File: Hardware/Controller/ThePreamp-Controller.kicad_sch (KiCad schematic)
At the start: 12 parts, among them J1 8V, J2 Digital Out, J3 SPI DISPLAY 1, J4 SPI DISPLAY 2, J5 Power relay trigger, SW1 RotaryEncoder_Switch, SW2 RotaryEncoder_Switch, U1 24C02C_SN, U2 ESP32-DEVKIT-V1, U3 TSOP34838, U4 PC817

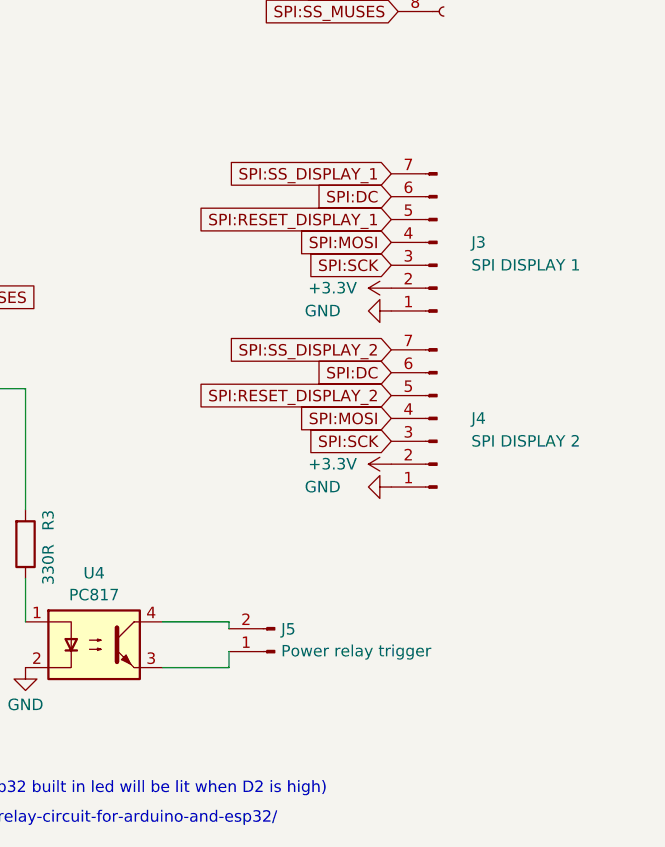
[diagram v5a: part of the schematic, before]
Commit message: Added symbol/footprint for display
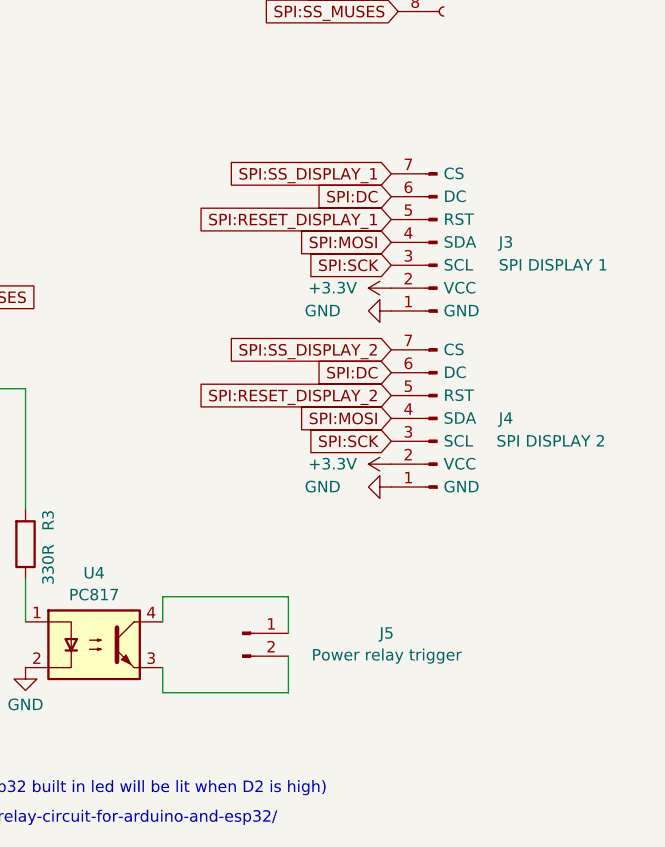
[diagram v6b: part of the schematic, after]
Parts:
- J3, J4: footprint Connector_PinHeader_2.54mm:PinHeader_1x07_P2.54mm_Vertical -> OLED SPI 2.08:OLED SPI 2.08; symbol Connector:Conn_01x07_Pin -> OLED SPI 2.08:OLED SPI 2.08
- J5: footprint Connector_JST:JST_XH_B2B-XH-AM_1x02_P2.50mm_Vertical -> Connector_JST:JST_XH_B2B-XH-A_1x02_P2.50mm_Vertical
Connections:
- net at U4.3: now also J5.2 (Pin_2); no longer J5.1 (Pin_1)
- net at U4.4: now also J5.1 (Pin_1); no longer J5.2 (Pin_2)
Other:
- moved on the sheet: J5
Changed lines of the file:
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@@
   (no_connect (at 157.48 76.2))
   (no_connect (at 157.48 73.66))
+  (wire (pts (xy 230.886 128.778) (xy 230.886 124.714))
+    (stroke (width 0) (type default))
+  )
   (wire (pts (xy 187.96 101.6) (xy 201.676 101.6))
     (stroke (width 0) (type default))
   )
-  (wire (pts (xy 216.916 127.508) (xy 224.282 127.508))
+  (wire (pts (xy 230.886 135.382) (xy 230.886 131.318))
     (stroke (width 0) (type default))
   )
@@
     (stroke (width 0) (type default))
   )
+  (wire (pts (xy 216.916 135.382) (xy 230.886 135.382))
+    (stroke (width 0) (type default))
+  )
   (wire (pts (xy 100.33 35.56) (xy 100.33 34.29))
     (stroke (width 0) (type default))
   )
+  (wire (pts (xy 216.916 124.714) (xy 230.886 124.714))
+    (stroke (width 0) (type default))
+  )
+  (wire (pts (xy 216.916 124.714) (xy 216.916 127.508))
+    (stroke (width 0) (type default))
+  )
   (wire (pts (xy 158.496 55.372) (xy 158.496 52.832))
     (stroke (width 0) (type default))
   )
-  (wire (pts (xy 224.282 130.81) (xy 224.282 132.588))
-    (stroke (width 0) (type default))
-  )
   (wire (pts (xy 158.496 50.292) (xy 158.496 52.832))
     (stroke (width 0) (type default))
@@
     (stroke (width 0) (type default))
   )
-  (wire (pts (xy 224.282 132.588) (xy 216.916 132.588))
-    (stroke (width 0) (type default))
-  )
   (wire (pts (xy 102.87 34.29) (xy 102.87 35.56))
     (stroke (width 0) (type default))
@@
     (stroke (width 0) (type default))
   )
-  (wire (pts (xy 224.282 127.508) (xy 224.282 128.27))
+  (wire (pts (xy 216.916 132.588) (xy 216.916 135.382))
     (stroke (width 0) (type default))
   )
@@
     )
   )
-  (symbol (lib_id "Connector:Conn_01x07_Pin") (at 247.396 85.344 180) (unit 1)
-    (in_bom yes) (on_board yes) (dnp no)
-    (property "Reference" "J3" (at 251.206 85.344 0)
-      (effects (font (size 1.27 1.27)) (justify right))
-    )
-    (property "Value" "SPI DISPLAY 1" (at 251.206 87.884 0)
-      (effects (font (size 1.27 1.27)) (justify right))
-    )
-    (property "Footprint" "Connector_PinHeader_2.54mm:PinHeader_1x07_P2.54mm_Vertical" (at 247.396 85.344 0)
+  (symbol (lib_id "OLED SPI 2.08:OLED SPI 2.08") (at 247.396 85.344 180) (unit 1)
+    (in_bom yes) (on_board yes) (dnp no)
+    (property "Reference" "J3" (at 254.254 85.344 0)
+      (effects (font (size 1.27 1.27)) (justify right))
+    )
+    (property "Value" "SPI DISPLAY 1" (at 254.254 87.884 0)
+      (effects (font (size 1.27 1.27)) (justify right))
+    )
+    (property "Footprint" "OLED SPI 2.08:OLED SPI 2.08" (at 223.266 75.184 0)
       (effects (font (size 1.27 1.27)) hide)
     )
@@
     )
   )
-  (symbol (lib_id "Connector:Conn_01x02_Pin") (at 229.362 130.81 180) (unit 1)
-    (in_bom yes) (on_board yes) (dnp no) (fields_autoplaced)
-    (property "Reference" "J5" (at 230.0732 128.3279 0)
-      (effects (font (size 1.27 1.27)) (justify right))
-    )
-    (property "Value" "Power relay trigger" (at 230.0732 130.7521 0)
-      (effects (font (size 1.27 1.27)) (justify right))
-    )
-    (property "Footprint" "Connector_JST:JST_XH_B2B-XH-AM_1x02_P2.50mm_Vertical" (at 229.362 130.81 0)
-      (effects (font (size 1.27 1.27)) hide)
-    )
-    (property "Datasheet" "~" (at 229.362 130.81 0)
+  (symbol (lib_id "Connector:Conn_01x02_Pin") (at 225.806 128.778 0) (unit 1)
+    (in_bom yes) (on_board yes) (dnp no)
+    (property "Reference" "J5" (at 241.808 128.778 0)
+      (effects (font (size 1.27 1.27)))
+    )
+    (property "Value" "Power relay trigger" (at 241.808 131.2022 0)
+      (effects (font (size 1.27 1.27)))
+    )
+    (property "Footprint" "Connector_JST:JST_XH_B2B-XH-A_1x02_P2.50mm_Vertical" (at 225.806 128.778 0)
+      (effects (font (size 1.27 1.27)) hide)
+    )
+    (property "Datasheet" "~" (at 225.806 128.778 0)
       (effects (font (size 1.27 1.27)) hide)
     )
@@
     )
   )
-  (symbol (lib_id "Connector:Conn_01x07_Pin") (at 247.396 104.902 180) (unit 1)
-    (in_bom yes) (on_board yes) (dnp no)
-    (property "Reference" "J4" (at 251.206 104.902 0)
-      (effects (font (size 1.27 1.27)) (justify right))
-    )
-    (property "Value" "SPI DISPLAY 2" (at 251.206 107.442 0)
-      (effects (font (size 1.27 1.27)) (justify right))
-    )
-    (property "Footprint" "Connector_PinHeader_2.54mm:PinHeader_1x07_P2.54mm_Vertical" (at 247.396 104.902 0)
-      (effects (font (size 1.27 1.27)) hide)
-    )
+  (symbol (lib_id "OLED SPI 2.08:OLED SPI 2.08") (at 247.396 104.902 180) (unit 1)
+    (in_bom yes) (on_board yes) (dnp no)
+    (property "Reference" "J4" (at 254.254 104.902 0)
+      (effects (font (size 1.27 1.27)) (justify right))
+    )
+    (property "Value" "SPI DISPLAY 2" (at 254 107.442 0)
+      (effects (font (size 1.27 1.27)) (justify right))
+    )
+    (property "Footprint" "OLED SPI 2.08:OLED SPI 2.08" (at 223.266 94.742 0)
+      (effects (font (size 1.27 1.27)) hide)
+    )

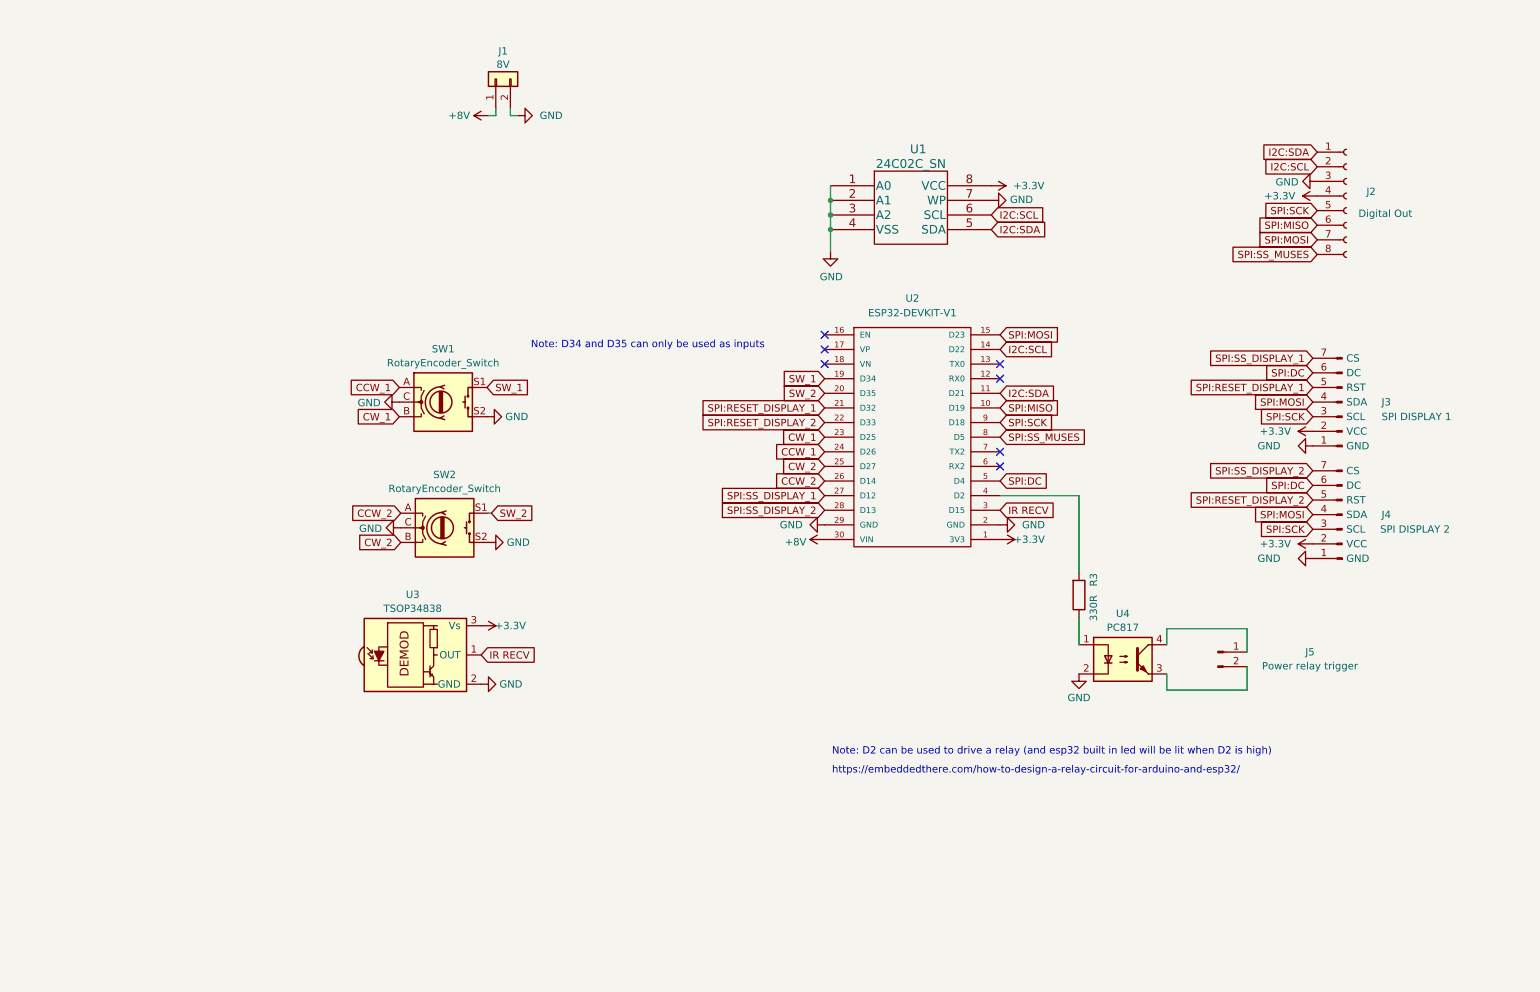
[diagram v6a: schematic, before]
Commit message: Controller pcb is ready (except for connectors)
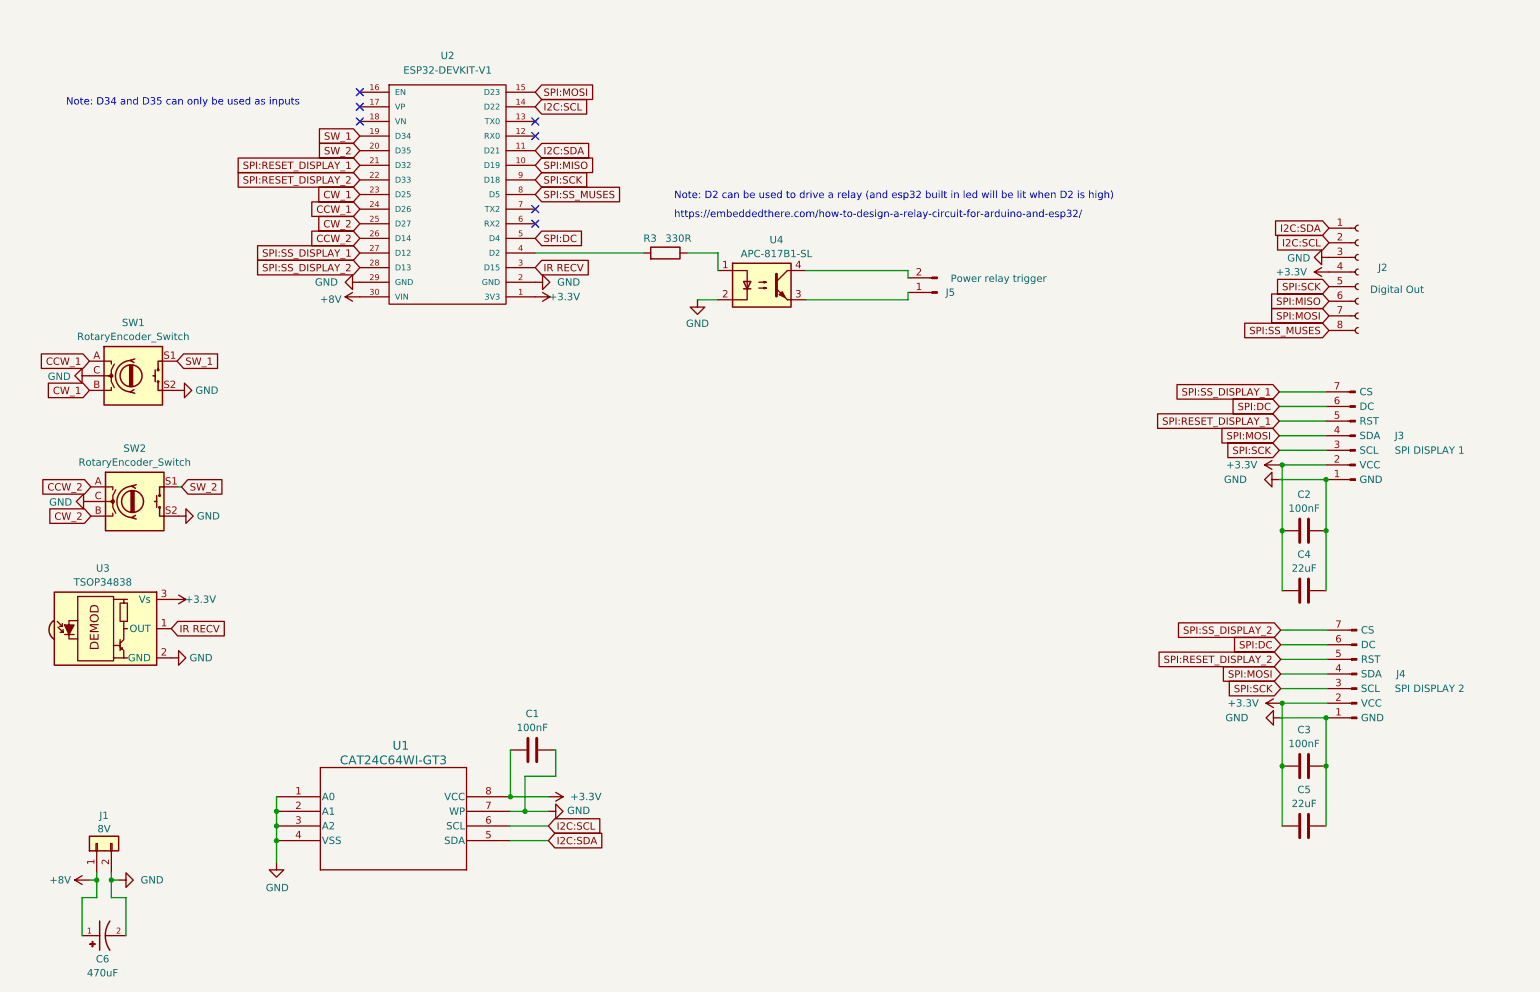
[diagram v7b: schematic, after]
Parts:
- added C1, C2, C3: 100nF, Capacitor_SMD:C_0805_2012Metric_Pad1.18x1.45mm_HandSolder, symbol Device:C
- added C4, C5: 22uF, Capacitor_SMD:C_1206_3216Metric_Pad1.33x1.80mm_HandSolder, symbol Device:C
- added C6: 470uF, EEE_FH1C471L:CAP_EEEFH1C471L, symbol EEE_FH1C471L:EEEFH1C471L
- U1: value 24C02C_SN -> CAT24C64WI-GT3; footprint Package_SO:SOIC-8-1EP_3.9x4.9mm_P1.27mm_EP2.41x3.3mm -> footprints:SOIC8_ONS-M; symbol Mezmerize_B1_Controller-rescue:24C02C_SN-24C02 -> CAT24C64WI_GT3:CAT24C64WI-GT3
- U4: value PC817 -> APC-817B1-SL; footprint Package_DIP:DIP-4_W7.62mm -> APC_817B1_SL:APC-817xx-SL_AMB-M
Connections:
- net +3V3: now also C1.1, C2.1, C3.1, C4.1, C5.1
- net +8V: now also C6.1
- net GND: now also C1.2, C2.2, C3.2, C4.2, C5.2, C6.2
- net at U4.3: now also J5.1 (Pin_1); no longer J5.2 (Pin_2)
- net at U4.4: now also J5.2 (Pin_2); no longer J5.1 (Pin_1)
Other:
- moved on the sheet: J1, J2, J3, J4, J5, R3, SW1, SW2, U2, U3, U4

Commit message: Digital connector (IDC 16) aligned on controller and analog board
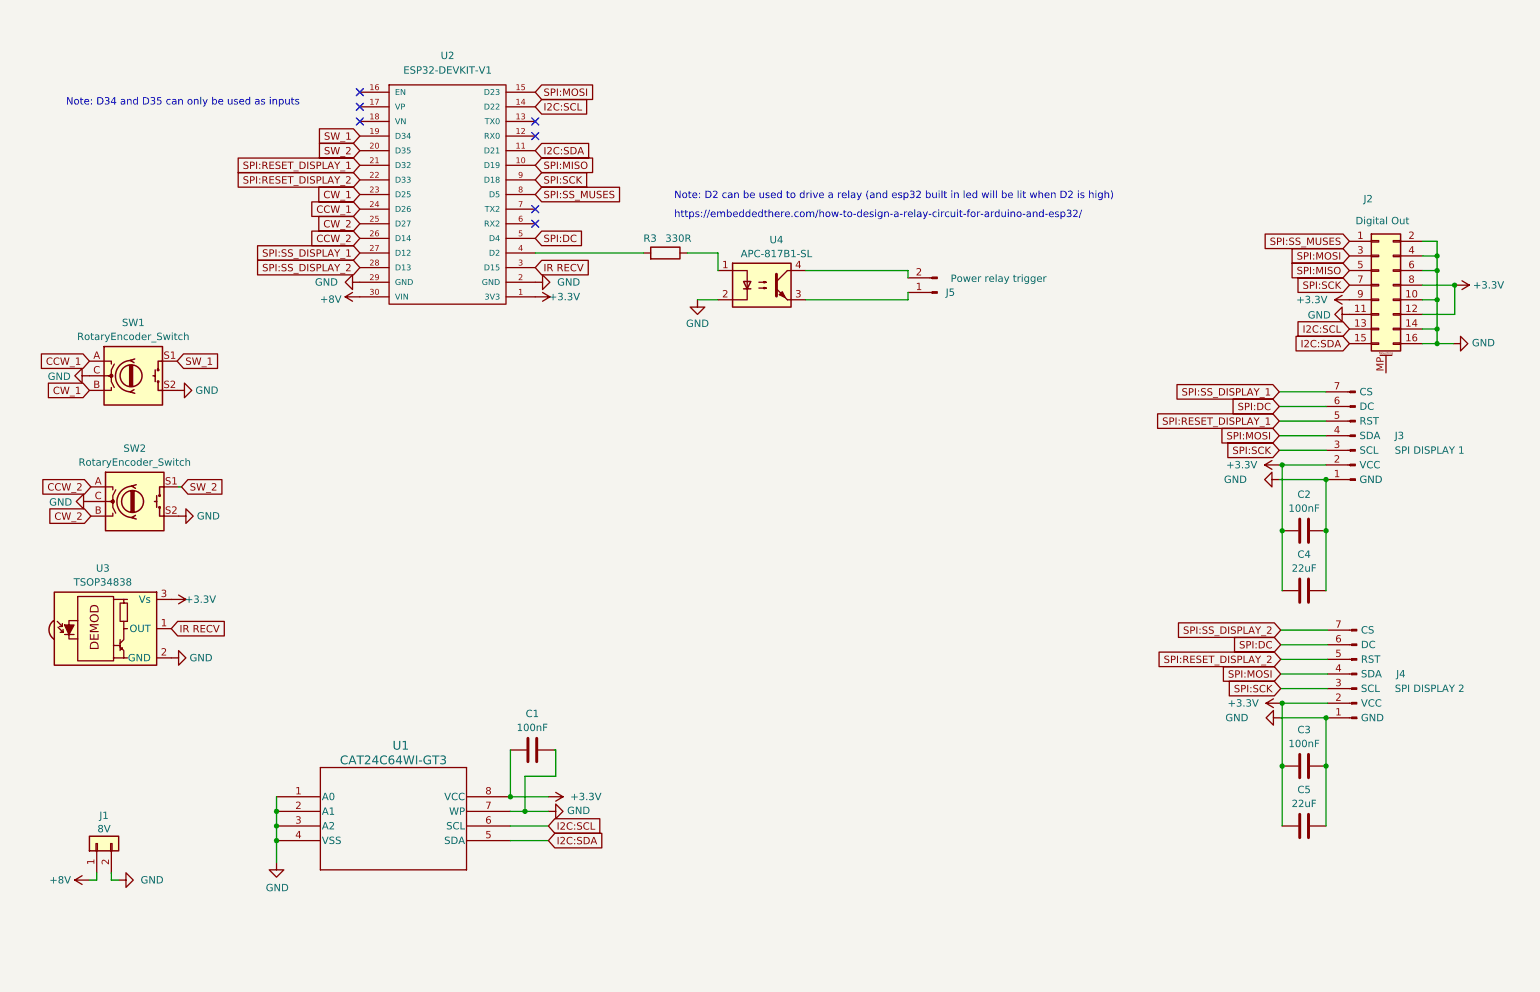
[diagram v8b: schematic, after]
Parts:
- removed C6: 470uF, EEE_FH1C471L:CAP_EEEFH1C471L, symbol EEE_FH1C471L:EEEFH1C471L
- removed J2: Digital Out, Connector_JST:JST_XH_B8B-XH-A_1x08_P2.50mm_Vertical, symbol Connector:Conn_01x08_Female
- added J2: Digital Out, Connector_IDC:IDC-Header_2x08_P2.54mm_Vertical, symbol Connector_Generic_MountingPin:Conn_02x08_Odd_Even_MountingPin
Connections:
- net +3V3: now also J2.12 (Pin_12), J2.8 (Pin_8), J2.9 (Pin_9)
- net GND: now also J2.10 (Pin_10), J2.11 (Pin_11), J2.14 (Pin_14), J2.16 (Pin_16), J2.2 (Pin_2), J2.4 (Pin_4), J2.6 (Pin_6)
- net I2C:SCL: now also J2.13 (Pin_13)
- net I2C:SDA: now also J2.15 (Pin_15)
- net SPI:MISO: now also J2.5 (Pin_5)
- net SPI:MOSI: now also J2.3 (Pin_3)
- net SPI:SCK: now also J2.7 (Pin_7)
- net SPI:SS_MUSES: now also J2.1 (Pin_1)
